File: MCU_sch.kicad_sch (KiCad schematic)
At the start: 17 parts

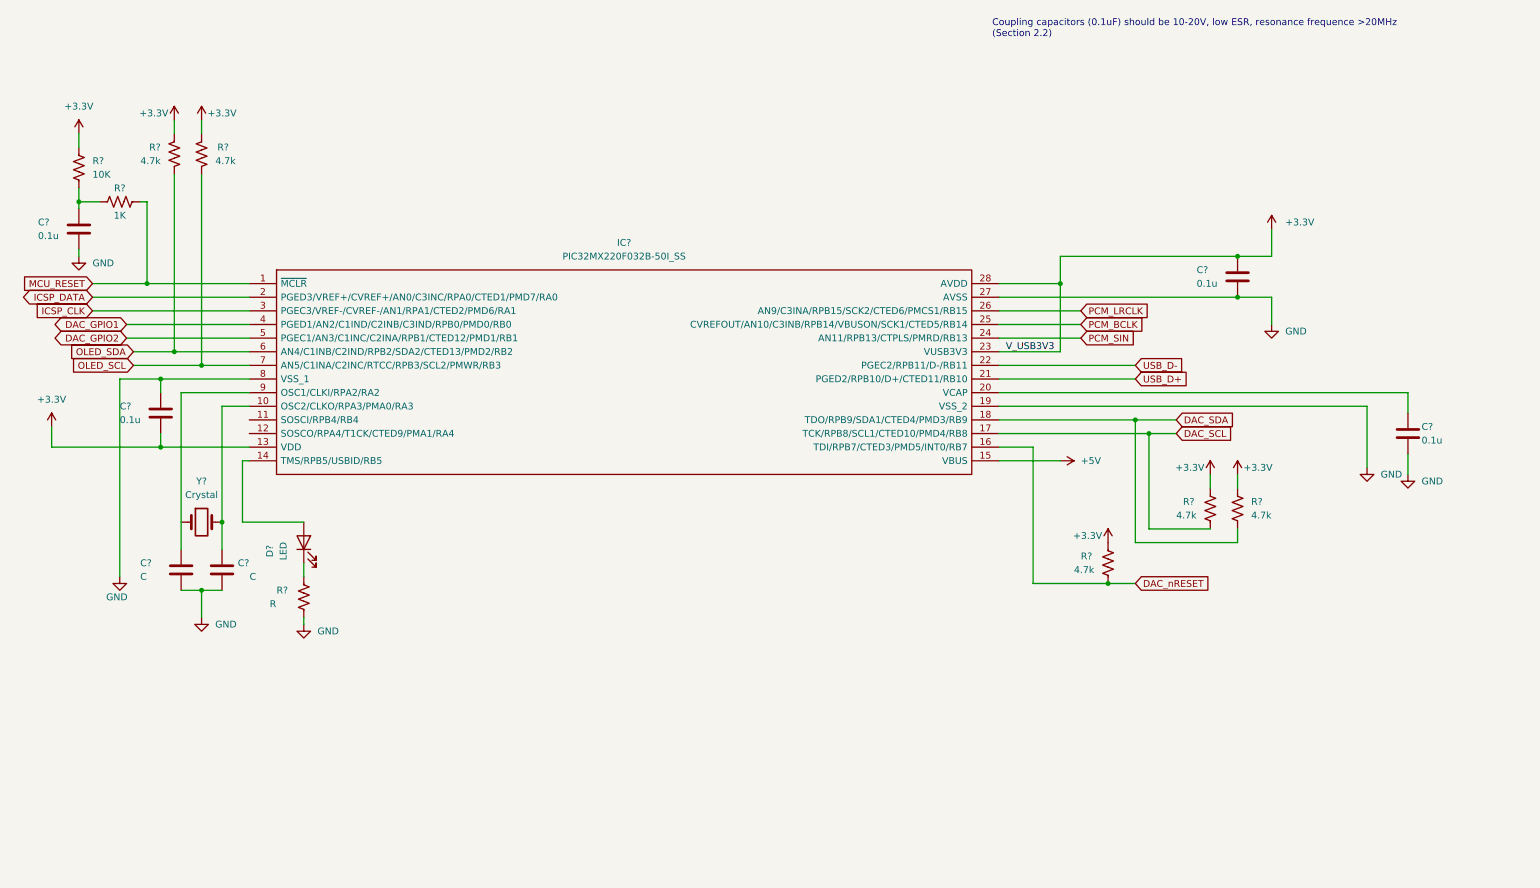
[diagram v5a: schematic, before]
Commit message: Finishing Schematic. Fixed ERC errors
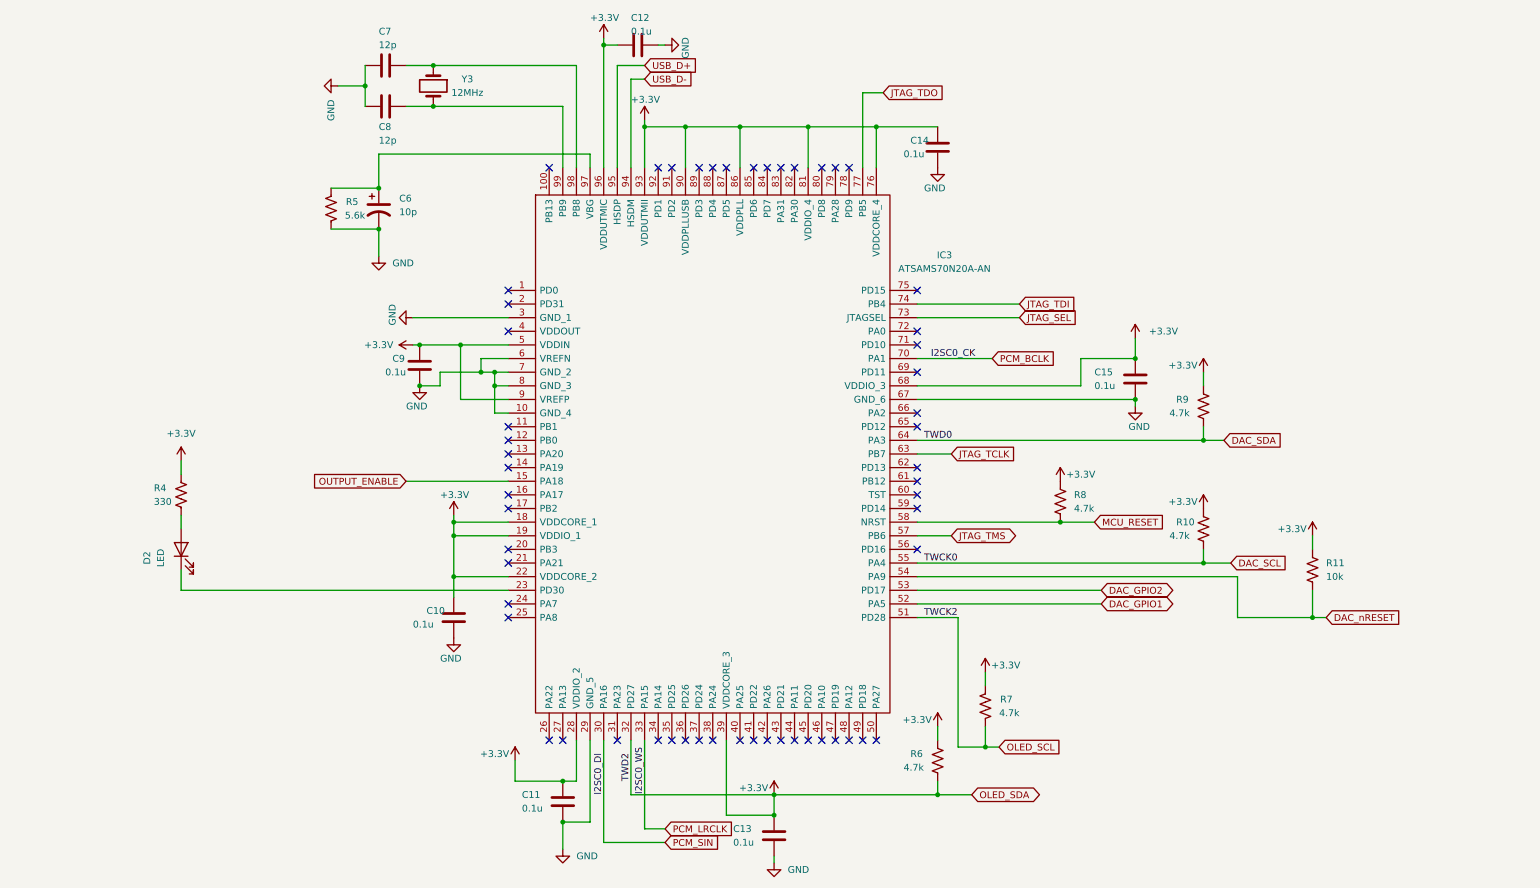
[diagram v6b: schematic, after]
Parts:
- removed C?: C, symbol Device:C
- removed C? (x3): 0.1u, symbol Device:C
- removed IC?: PIC32MX220F032B-50I_SS, SOP65P780X200-28N, symbol SamacSys_Parts:PIC32MX220F032B-50I_SS
- removed R?: 10K, symbol Device:R_US
- removed R? (x2): 4.7k, symbol Device:R_US
- removed R?: 1K, symbol Device:R_US
- added C10, C11, C12, C13, C14, C9: 0.1u, symbol Device:C
- added C6: 10p, symbol Device:C_Polarized_US
- added C8: 12p, symbol Device:C
- added IC3: ATSAMS70N20A-AN, QFP50P1600X1600X160-100N, symbol SamacSys_Parts:ATSAMS70N20A-AN
- added R11: 10k, symbol Device:R_US
- added R5: 5.6k, symbol Device:R_US
- added R6, R7: 4.7k, symbol Device:R_US
- C7: renamed from C?; value C -> 12p
- R4: renamed from R?; value R -> 330
- Y3: renamed from Y?; value Crystal -> 12MHz
- gave numbers to parts that had none: 5
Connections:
- net +3V3: now also C15.1, R4.1, C10.1, C11.1, C12.2, C13.1, C14.1, C9.1, IC3.18 (VDDCORE_1), IC3.19 (VDDIO_1), IC3.22 (VDDCORE_2), IC3.28 (VDDIO_2), IC3.32 (PD27), IC3.39 (VDDCORE_3), IC3.5 (VDDIN), IC3.68 (VDDIO_3), IC3.76 (VDDCORE_4), IC3.81 (VDDIO_4), IC3.86 (VDDPLL), IC3.9 (VREFP), IC3.90 (VDDPLLUSB), IC3.93 (VDDUTMII), IC3.96 (VDDUTMIC), R11.1, R6.1, R6.2, R7.1; no longer C15.2
- net DAC_GPIO1: now also IC3.52 (PA5)
- net DAC_GPIO2: now also IC3.53 (PD17)
- net DAC_SCL: now also R10.2, IC3.55 (PA4); no longer R9.2
- net DAC_SDA: now also R9.2, IC3.64 (PA3); no longer R8.2
- net DAC_nRESET: now also IC3.54 (PA9), R11.2; no longer R10.2
- net GND: now also C15.2, C10.2, C11.2, C12.1, C13.2, C14.2, C6.2, C8.2, C9.2, IC3.10 (GND_4), IC3.29 (GND_5), IC3.3 (GND_1), IC3.6 (VREFN), IC3.67 (GND_6), IC3.7 (GND_2), IC3.8 (GND_3), R5.2; no longer C15.1, R4.2
- net MCU_RESET: now also R8.2, IC3.58 (NRST)
- net OLED_SCL: now also IC3.51 (PD28), R7.2
- net PCM_BCLK: now also IC3.70 (PA1)
- net PCM_LRCLK: now also IC3.33 (PA15)
- net PCM_SIN: now also IC3.30 (PA16)
- net USB_D+: now also IC3.95 (HSDP)
- net USB_D-: now also IC3.94 (HSDM)
- net at Y3.2: now also C8.1, IC3.99 (PB9)
- net at C7.1: now also Y3.1, IC3.98 (PB8)
- net at D2.1 (K): now also IC3.23 (PD30); no longer R4.1
- net at D2.2 (A): now also R4.2
- new net: C6.1, IC3.97 (VBG), R5.1
- new net JTAG_SEL: IC3.73 (JTAGSEL)
- new net JTAG_TCLK: IC3.63 (PB7)
- new net JTAG_TDI: IC3.74 (PB4)
- new net JTAG_TDO: IC3.77 (PB5)
- new net JTAG_TMS: IC3.57 (PB6)
- new net OUTPUT_ENABLE: IC3.15 (PA18)
- no-connect marks 0 -> 56
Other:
- note removed: "Coupling capacitors (0.1uF) should be 10-20V, low ESR, resonance frequence >20MHz (Section 2.2)"
- moved on the sheet: C15, C7, D2, R10, R4, R8, R9, Y3

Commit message: Adding footprints
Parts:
- C10, C11, C12, C13, C14, C15, C6, C7, C8, C9: footprint (none) -> Capacitor_SMD:C_0805_2012Metric_Pad1.18x1.45mm_HandSolder
- D2: footprint (none) -> LED_SMD:LED_0805_2012Metric_Pad1.15x1.40mm_HandSolder
- IC3: footprint QFP50P1600X1600X160-100N -> SamacSys_Parts:QFP50P1600X1600X160-100N
- R10, R11, R4, R5, R6, R7, R8, R9: footprint (none) -> Resistor_SMD:R_0805_2012Metric_Pad1.20x1.40mm_HandSolder
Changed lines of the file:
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@@
       (effects (font (size 1.27 1.27)) (justify left))
     )
-    (property "Footprint" "" (id 2) (at 98.7552 129.54 0)
+    (property "Footprint" "Capacitor_SMD:C_0805_2012Metric_Pad1.18x1.45mm_HandSolder" (id 2) (at 98.7552 129.54 0)
       (effects (font (size 1.27 1.27)) hide)
     )
@@
       (effects (font (size 1.27 1.27)) (justify left))
     )
-    (property "Footprint" "" (id 2) (at 211.836 104.394 90)
+    (property "Footprint" "Resistor_SMD:R_0805_2012Metric_Pad1.20x1.40mm_HandSolder" (id 2) (at 211.836 104.394 90)
       (effects (font (size 1.27 1.27)) hide)
     )
@@
       (effects (font (size 1.27 1.27)) (justify left))
     )
-    (property "Footprint" "" (id 2) (at 128.27 20.0152 0)
+    (property "Footprint" "Capacitor_SMD:C_0805_2012Metric_Pad1.18x1.45mm_HandSolder" (id 2) (at 128.27 20.0152 0)
       (effects (font (size 1.27 1.27)) hide)
     )
@@
       (effects (font (size 1.27 1.27)) (justify left))
     )
-    (property "Footprint" "" (id 2) (at 225.7552 85.09 0)
+    (property "Footprint" "Capacitor_SMD:C_0805_2012Metric_Pad1.18x1.45mm_HandSolder" (id 2) (at 225.7552 85.09 0)
       (effects (font (size 1.27 1.27)) hide)
     )
@@
       (effects (font (size 1.27 1.27)) (justify left))
     )
-    (property "Footprint" "" (id 2) (at 258.826 117.094 90)
+    (property "Footprint" "Resistor_SMD:R_0805_2012Metric_Pad1.20x1.40mm_HandSolder" (id 2) (at 258.826 117.094 90)
       (effects (font (size 1.27 1.27)) hide)
     )
@@
       (effects (font (size 1.27 1.27)) (justify left))
     )
-    (property "Footprint" "" (id 2) (at 188.976 152.654 90)
+    (property "Footprint" "Resistor_SMD:R_0805_2012Metric_Pad1.20x1.40mm_HandSolder" (id 2) (at 188.976 152.654 90)
       (effects (font (size 1.27 1.27)) hide)
     )
@@
       (effects (font (size 1.27 1.27)) (justify left))
     )
-    (property "Footprint" "" (id 2) (at 81.28 31.4452 0)
+    (property "Footprint" "Capacitor_SMD:C_0805_2012Metric_Pad1.18x1.45mm_HandSolder" (id 2) (at 81.28 31.4452 0)
       (effects (font (size 1.27 1.27)) hide)
     )
@@
       (effects (font (size 1.27 1.27)) (justify left))
     )
-    (property "Footprint" "" (id 2) (at 119.0752 163.83 0)
+    (property "Footprint" "Capacitor_SMD:C_0805_2012Metric_Pad1.18x1.45mm_HandSolder" (id 2) (at 119.0752 163.83 0)
       (effects (font (size 1.27 1.27)) hide)
     )
@@
       (effects (font (size 1.27 1.27)) (justify left))
     )
-    (property "Footprint" "" (id 2) (at 83.82 49.53 0)
+    (property "Footprint" "Capacitor_SMD:C_0805_2012Metric_Pad1.18x1.45mm_HandSolder" (id 2) (at 83.82 49.53 0)
       (effects (font (size 1.27 1.27)) hide)
     )
@@
       (effects (font (size 1.27 1.27)) (justify left))
     )
-    (property "Footprint" "" (id 2) (at 81.28 23.8252 0)
+    (property "Footprint" "Capacitor_SMD:C_0805_2012Metric_Pad1.18x1.45mm_HandSolder" (id 2) (at 81.28 23.8252 0)
       (effects (font (size 1.27 1.27)) hide)
     )
@@
       (effects (font (size 1.27 1.27)) (justify left))
     )
-    (property "Footprint" "" (id 2) (at 195.834 142.494 90)
+    (property "Footprint" "Resistor_SMD:R_0805_2012Metric_Pad1.20x1.40mm_HandSolder" (id 2) (at 195.834 142.494 90)
       (effects (font (size 1.27 1.27)) hide)
     )
@@
     (property "Reference" "D2" (id 0) (at 40.64 114.6175 0))
     (property "Value" "LED" (id 1) (at 43.18 114.6175 0))
-    (property "Footprint" "" (id 2) (at 46.99 113.03 0)
+    (property "Footprint" "LED_SMD:LED_0805_2012Metric_Pad1.15x1.40mm_HandSolder" (id 2) (at 46.99 113.03 0)
       (effects (font (size 1.27 1.27)) hide)
     )
@@
       (effects (font (size 1.27 1.27)) (justify left))
     )
-    (property "Footprint" "" (id 2) (at 158.4452 170.18 0)
+    (property "Footprint" "Capacitor_SMD:C_0805_2012Metric_Pad1.18x1.45mm_HandSolder" (id 2) (at 158.4452 170.18 0)
       (effects (font (size 1.27 1.27)) hide)
     )
@@
       (effects (font (size 1.27 1.27)) (justify left))
     )
-    (property "Footprint" "" (id 2) (at 188.9252 41.91 0)
+    (property "Footprint" "Capacitor_SMD:C_0805_2012Metric_Pad1.18x1.45mm_HandSolder" (id 2) (at 188.9252 41.91 0)
       (effects (font (size 1.27 1.27)) hide)
     )
@@
     (property "Reference" "IC3" (id 0) (at 189.23 58.1912 0))
     (property "Value" "ATSAMS70N20A-AN" (id 1) (at 189.23 60.7312 0))
-    (property "Footprint" "QFP50P1600X1600X160-100N" (id 2) (at 180.34 46.99 0)
+    (property "Footprint" "SamacSys_Parts:QFP50P1600X1600X160-100N" (id 2) (at 180.34 46.99 0)
       (effects (font (size 1.27 1.27)) (justify left) hide)
     )
@@
       (effects (font (size 1.27 1.27)) (justify left))
     )
-    (property "Footprint" "" (id 2) (at 238.506 109.474 90)
+    (property "Footprint" "Resistor_SMD:R_0805_2012Metric_Pad1.20x1.40mm_HandSolder" (id 2) (at 238.506 109.474 90)
       (effects (font (size 1.27 1.27)) hide)
     )
@@
       (effects (font (size 1.27 1.27)) (justify left))
     )
-    (property "Footprint" "" (id 2) (at 73.914 49.784 90)
+    (property "Footprint" "Resistor_SMD:R_0805_2012Metric_Pad1.20x1.40mm_HandSolder" (id 2) (at 73.914 49.784 90)
       (effects (font (size 1.27 1.27)) hide)
     )
@@
       (effects (font (size 1.27 1.27)) (justify right))
     )
-    (property "Footprint" "" (id 2) (at 92.4052 82.55 0)
+    (property "Footprint" "Capacitor_SMD:C_0805_2012Metric_Pad1.18x1.45mm_HandSolder" (id 2) (at 92.4052 82.55 0)
       (effects (font (size 1.27 1.27)) hide)
     )
@@
       (effects (font (size 1.27 1.27)) (justify left))
     )
-    (property "Footprint" "" (id 2) (at 48.006 103.124 90)
+    (property "Footprint" "Resistor_SMD:R_0805_2012Metric_Pad1.20x1.40mm_HandSolder" (id 2) (at 48.006 103.124 90)
       (effects (font (size 1.27 1.27)) hide)
     )
@@
       (effects (font (size 1.27 1.27)) (justify left))
     )
-    (property "Footprint" "" (id 2) (at 238.506 86.614 90)
-      (effects (font (size 1.27 1.27)) hide)
-    )
+    (property "Footprint" "Resistor_SMD:R_0805_2012Metric_Pad1.20x1.40mm_HandSolder" (id 2) (at 238.506 86.614 90)
+      (effects (font (size 1.27 1.27)) hide)
+    )
